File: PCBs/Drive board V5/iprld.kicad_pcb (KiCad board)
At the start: 2 copper layers, 17 parts, among them J1 Conn_01x02, J2 Conn_02x01, J3 Conn_02x02_Top_Bottom, U1 TJA1051T-3, U15 AMS1117-3.3

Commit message: Updated drive board
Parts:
- removed C14, C26: 10u, Capacitor_SMD:C_0805_2012Metric
- removed C15: 1u, Capacitor_SMD:C_0805_2012Metric
- removed C21: 0.1u, Capacitor_SMD:C_0805_2012Metric
- removed U15: AMS1117-3.3, Package_TO_SOT_SMD:SOT-223-3_TabPin2
- added C3: 0.1u, Capacitor_SMD:C_0805_2012Metric, F.Cu at (43.0, 54.8)
- moved G*** 45.6 mm to (102.0, 97.2)
- moved C1 20.0 mm to (43.0, 50.2), turned to 0 degrees
- moved J3 15.4 mm to (103.0, 28.1)
- moved J1 13.3 mm to (91.5, 32.2)
- moved U1 12.9 mm to (41.3, 42.0), turned to 90 degrees
- moved C2 11.9 mm to (45.5, 34.2)
- moved J2 3.50 mm to (39.0, 28.1)
- moved U2 0.67 mm to (76.4, 66.4)
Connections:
- net /CANH renamed /CAN_P
- net /CANL renamed /CAN_N
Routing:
- net +3.3V: track 114.2 -> 50.0 mm, vias 1 -> 0
- net GND: track 49.2 -> 5.37 mm, vias 11 -> 3
- net /CAN_S: track 38.1 -> 0.00 mm
- net +5V: track 90.4 -> 71.0 mm, vias 0 -> 1
- net /CAN_RX: track 38.7 -> 21.1 mm
- net /M3: track 22.4 -> 33.9 mm
- net /M2: track 29.2 -> 40.1 mm
- net /M4: track 31.3 -> 40.1 mm
- net /CAN_N: track 6.53 -> 13.4 mm
- net /M1: track 30.5 -> 37.3 mm
- net /CAN_TX: track 25.9 -> 19.8 mm, vias 0 -> 1
- net /CAN_P: track 6.63 -> 9.14 mm

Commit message: Drive v5 changes
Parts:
- moved G*** 41.0 mm to (100.8, 56.2)
- moved H2 40.1 mm to (25.0, 73.5)
- moved H3 39.8 mm to (115.0, 73.8)
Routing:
- net /CAN_S: track 0.00 -> 37.7 mm, vias 0 -> 1
- net GND: track 5.37 -> 7.39 mm, vias 3 -> 4
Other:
- board outline added: 100 x 60 mm
- board text added: "CAN H"
- board text added: "CAN L"
- board text added: "Drive Board by Max Ryan :)"
- board text added: "Pineapple on pizza should be a crime"
- board text removed: "Drive Board by Max Ryan"
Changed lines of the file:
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@@
 	(footprint "footprints:IPRL_31mm"
 		(layer "F.Cu")
-		(at 102 97.25)
+		(at 100.75 56.25)
 		(property "Reference" "G***"
 			(at 0 0 0)
@@
 			(at -0.5 6.4 0)
 			(layer "F.SilkS")
+			(hide yes)
 			(effects
 				(font
@@
 			(at -2.75 -9.75 0)
 			(layer "F.SilkS")
+			(hide yes)
 			(effects
 				(font
@@
 	(footprint "MountingHole:MountingHole_3.2mm_M3_Pad_TopBottom"
 		(layer "F.Cu")
-		(at 25 113.6)
+		(at 25 73.5)
 		(descr "Mounting Hole 3.2mm, M3, generated by kicad-footprint-generator mountinghole.py")
 		(tags "mountinghole M3")
@@
 			(at 0 -4.15 0)
 			(layer "F.SilkS")
+			(hide yes)
 			(effects
 				(font
@@
 			(at 0 6.4 0)
 			(layer "F.SilkS")
+			(hide yes)
 			(effects
 				(font
@@
 	(footprint "MountingHole:MountingHole_3.2mm_M3_Pad_TopBottom"
 		(layer "F.Cu")
-		(at 115 113.6)
+		(at 115 73.75)
 		(descr "Mounting Hole 3.2mm, M3, generated by kicad-footprint-generator mountinghole.py")
 		(tags "mountinghole M3")
@@
 			(at 0 -4.15 0)
 			(layer "F.SilkS")
+			(hide yes)
 			(effects
 				(font
@@
 		(embedded_fonts no)
 	)
-	(gr_line
-		(start 20 18.6)
-		(end 25 18.6)
-		(stroke
-			(width 0.2)
-			(type default)
-		)
-		(layer "F.Cu")
-	)
-	(gr_line
-		(start 20 118.6)
-		(end 25 118.6)
-		(stroke
-			(width 0.2)
-			(type default)
-		)
-		(layer "F.Cu")
-	)
-	(gr_line
-		(start 120 18.6)
-		(end 114.9 18.6)
-		(stroke
-			(width 0.2)
-			(type default)
-		)
-		(layer "F.Cu")
-	)
-	(gr_line
-		(start 25 118.6)
-		(end 25 113.6)
-		(stroke
-			(width 0.2)
-			(type default)
-		)
-		(layer "F.Cu")
-	)
-	(gr_line
-		(start 120 118.6)
-		(end 115 118.6)
-		(stroke
-			(width 0.2)
-			(type default)
-		)
-		(layer "F.Cu")
-	)
-	(gr_line
-		(start 25 18.6)
-		(end 25 23.6)
-		(stroke
-			(width 0.2)
-			(type default)
-		)
-		(layer "F.Cu")
-	)
 	(gr_rect
 		(start 20 18.6)
-		(end 120 118.6)
+		(end 120 78.6)
 		(stroke
 			(width 0.2)
-			(type default)
+			(type solid)
 		)
 		(fill no)
-		(layer "F.Cu")
+		(layer "Edge.Cuts")
 	)
-	(gr_line
-		(start 115 118.6)
-		(end 115 113.6)
-		(stroke
-			(width 0.2)
-			(type default)
+	(gr_text "Pineapple \non pizza \nshould be \na crime"
+		(at 85.25 26.25 0)
+		(layer "F.SilkS")
+		(effects
+			(font
+				(size 1 1)
+				(thickness 0.1)
+			)
+			(justify left bottom)
 		)
-		(layer "F.Cu")
 	)
-	(gr_line
-		(start 120 23.6)
-		(end 115 23.6)
-		(stroke
-			(width 0.2)
-			(type default)
+	(gr_text "Drive Board\nby Max Ryan :)"
+		(at 91 72 0)
+		(layer "F.SilkS")
+		(effects
+			(font
+				(size 1.5 1.5)
+				(thickness 0.3)
+				(bold yes)
+			)
+			(justify left bottom)
 		)
-		(layer "F.Cu")
 	)
-	(gr_line
-		(start 120 18.6)
-		(end 120 23.6)
-		(stroke
-			(width 0.2)
-			(type default)
+	(gr_text "CAN L\n"
+		(at 42.685 28.25 0)
+		(layer "F.SilkS")
+		(effects
+			(font
+				(size 1 1)
+				(thickness 0.1)
+			)
+			(justify left bottom)
 		)
-		(layer "F.Cu")
 	)
-	(gr_text "Drive Board\nby Max Ryan"
-		(at 93.5 116 0)
+	(gr_text "CAN H\n"
+		(at 32.75 31.75 0)
 		(layer "F.SilkS")
 		(effects
 			(font
-				(size 1.5 1.5)
-				(thickness 0.3)
-				(bold yes)
+				(size 1 1)
+				(thickness 0.1)
 			)
 			(justify left bottom)
@@
 	)
 	(segment
+		(start 46.45 34.25)
+		(end 46.45 32.3)
+		(width 0.2)
+		(layer "F.Cu")
+		(net 1)
+	)
+	(segment
 		(start 43.95 50.25)
 		(end 45.25 50.25)
@@
 	)
 	(segment
+		(start 46.45 32.3)
+		(end 46.5 32.25)
+		(width 0.2)
+		(layer "F.Cu")
+		(net 1)
+	)
+	(segment
 		(start 44 54.75)
 		(end 45.5 54.75)
@@
 	)
 	(via
+		(at 46.5 32.25)
+		(size 0.6)
+		(drill 0.3)
+		(layers "F.Cu" "B.Cu")
+		(net 1)
+	)
+	(via
 		(at 40.75 47)
 		(size 0.6)
@@
 	(segment
 		(start 39.45 32.106339)
-		(end 39.45 36.97)
+		(end 40.051 31.505339)
 		(width 0.2)
 		(layer "F.Cu")
@@
 	)
 	(segment
-		(start 41.311 38.831)
-		(end 41.98 39.5)
+		(start 39.45 28.52)
+		(end 39 28.07)
 		(width 0.2)
 		(layer "F.Cu")
@@
 	)
 	(segment
-		(start 39.45 36.97)
-		(end 40.704 38.224)
+		(start 40.704 38.224)
+		(end 39.45 36.97)
 		(width 0.2)
 		(layer "F.Cu")
@@
 	)
 	(segment
-		(start 41.050968 38.224)
-		(end 41.311 38.484032)
+		(start 40.051 31.505339)
+		(end 40.051 30.634661)
 		(width 0.2)
 		(layer "F.Cu")
@@
 	)
 	(segment
-		(start 40.051 31.505339)
-		(end 39.45 32.106339)
+		(start 41.311 38.831)
+		(end 41.311 38.484032)
 		(width 0.2)
 		(layer "F.Cu")
@@
 	)
 	(segment
-		(start 39 28.07)
-		(end 39.45 28.52)
+		(start 41.98 39.5)
+		(end 41.311 38.831)
 		(width 0.2)
 		(layer "F.Cu")
@@
 	)
 	(segment
-		(start 39.45 28.52)
-		(end 39.45 30.033661)
+		(start 41.050968 38.224)
+		(end 40.704 38.224)
 		(width 0.2)
 		(layer "F.Cu")
@@
 	(segment
 		(start 39.45 30.033661)
-		(end 40.051 30.634661)
+		(end 39.45 28.52)
 		(width 0.2)
 		(layer "F.Cu")
@@
 	)
 	(segment
-		(start 40.704 38.224)
+		(start 39.45 35.27492)
+		(end 39.45 32.106339)
+		(width 0.2)
+		(layer "F.Cu")
+		(net 19)
+	)
+	(segment
+		(start 41.311 38.484032)
 		(end 41.050968 38.224)
 		(width 0.2)
@@
 	)
 	(segment
-		(start 40.051 30.634661)
-		(end 40.051 31.505339)
+		(start 39.45 36.97)
+		(end 39.45 35.27492)
 		(width 0.2)
 		(layer "F.Cu")
@@
 	)
 	(segment
-		(start 41.311 38.484032)
-		(end 41.311 38.831)
+		(start 40.051 30.634661)
+		(end 39.45 30.033661)
 		(width 0.2)
 		(layer "F.Cu")
@@
 	)
 	(segment
-		(start 39 31.07)
+		(start 40.43597 38.592367)
 		(end 39 37.156397)
 		(width 0.2)
@@
 	)
 	(segment
-		(start 39 37.156397)
+		(start 39 35.27492)
+		(end 39 31.07)
+		(width 0.2)
+		(layer "F.Cu")
+		(net 20)
+	)
+	(segment
+		(start 40.71 39.5)
 		(end 40.71 38.866397)
 		(width 0.2)
@@
 	)
 	(segment
+		(start 39 37.156397)
+		(end 39 35.27492)
+		(width 0.2)
+		(layer "F.Cu")
+		(net 20)
+	)
+	(segment
 		(start 40.71 38.866397)
-		(end 40.71 39.5)
+		(end 40.43597 38.592367)
 		(width 0.2)
 		(layer "F.Cu")
@@
 	)
 	(segment
+		(start 39.44 39.5)
+		(end 36 42.94)
+		(width 0.2)
+		(layer "F.Cu")
+		(net 26)
+	)
+	(segment
+		(start 36 42.94)
+		(end 36 43.5)
+		(width 0.2)
+		(layer "F.Cu")
+		(net 26)
+	)
+	(via
+		(at 36 43.5)
+		(size 0.6)
+		(drill 0.3)
+		(layers "F.Cu" "B.Cu")
+		(net 26)
+	)
+	(segment
+		(start 36 43.5)
+		(end 36 54.25)
+		(width 0.2)
+		(layer "B.Cu")
+		(net 26)
+	)
+	(segment
+		(start 36 54.25)
+		(end 45.62 63.87)
+		(width 0.2)
+		(layer "B.Cu")
+		(net 26)
+	)
+	(segment
+		(start 45.62 63.87)
+		(end 53.5 63.87)
+		(width 0.2)
+		(layer "B.Cu")
+		(net 26)
+	)
+	(segment
 		(start 50 57.83)
 		(end 53.5 61.33)
@@
 		)
 	)
+	(generated
+		(type tuning_pattern)
+		(name "Tuning Pattern")
+		(layer "F.Cu")
+		(base_line
+			(pts
+				(xy 40.43597 38.592367) (xy 39 37.156397) (xy 39 35.27492)
+			)
+		)
+		(base_line_coupled
+			(pts
+				(xy 40.704 38.224) (xy 39.45 36.97) (xy 39.45 35.27492)
+			)
+		)
+		(corner_radius_percent 80)
+		(end
+			(xy 39 35.27492)
+		)
+		(initial_side "left")
+		(last_diff_pair_gap 0.25)
+		(last_netname "/CAN_P")
+		(last_status "tuned")
+		(last_track_width 0.2)
+		(last_tuning "13.3037 mm (tuned)")
+		(max_amplitude 1)
+		(min_amplitude 0.2)
+		(min_spacing 1)
+		(origin
+			(xy 40.43597 38.592367)
+		)
+		(override_custom_rules no)
+		(rounded yes)
+		(single_sided no)
+		(target_length 1000000)
+		(target_length_max 1000000)
+		(target_length_min 0)
+		(target_skew 0)
+		(target_skew_max 0.1)
+		(target_skew_min -0.1)
+		(tuning_mode "diff_pair")
+		(members "356f25eb-2dce-41ec-9833-14f512c0acfb" "38f040bc-6008-4836-886b-c5aaa7f139b5"
+			"bcd30e06-786a-4961-932b-d6303e9b7a0b" "eff296ab-6fed-4a58-92bb-c176535c685c"
+		)
+	)

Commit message: Updates drive board
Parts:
- added G***: LOGO, LOGO, F.Cu at (37.3, 73.0)
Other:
- board text added: "What went wrong?"
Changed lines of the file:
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@@
+		(embedded_fonts no)
+	)
+	(footprint "LOGO"
+		(layer "F.Cu")
+		(at 37.306739 72.985484)
+		(property "Reference" "G***"
+			(at -1.5 -4.75 0)
+			(layer "F.SilkS")
+			(hide yes)
+			(effects
+				(font
+					(size 1.5 1.5)
+					(thickness 0.3)
+				)
+			)
+		)
+		(property "Value" "LOGO"
+			(at 0.75 0 0)
+			(layer "F.SilkS")
+			(hide yes)
+			(effects
+				(font
+					(size 1.5 1.5)
+					(thickness 0.3)
+				)
+			)
+		)
+		(property "Datasheet" ""
+			(at 0 0 0)
+			(layer "F.Fab")
+			(hide yes)
+			(effects
+				(font
+					(size 1.27 1.27)
+					(thickness 0.15)
+				)
+			)
+		)
+		(property "Description" ""
+			(at 0 0 0)
+			(layer "F.Fab")
+			(hide yes)
+			(effects
+				(font
+					(size 1.27 1.27)
+					(thickness 0.15)
+				)
+			)
+		)
+		(attr board_only exclude_from_pos_files exclude_from_bom)
+		(fp_poly
+			(pts
+				(xy -4.444145 4.932513) (xy -4.444145 5.000884) (xy -4.722515 5.000884) (xy -5.000884 5.000884)
+				(xy -5.000884 4.932513) (xy -5.000884 4.864141) (xy -4.722515 4.864141) (xy -4.444145 4.864141)
+			)
+			(stroke
+				(width 0)
+				(type solid)
+			)
+			(fill yes)
+			(layer "F.SilkS")
+		)
+		(fp_poly
+			(pts
+				(xy -3.61392 4.512517) (xy -3.61392 4.580888) (xy -3.889848 4.580888) (xy -4.165776 4.580888) (xy -4.165776 4.512517)
+				(xy -4.165776 4.444145) (xy -3.889848 4.444145) (xy -3.61392 4.444145)
+			)
+			(stroke
+				(width 0)
+				(type solid)
+			)
+			(fill yes)
+			(layer "F.SilkS")
+		)
+		(fp_poly
+			(pts
+				(xy -2.778812 3.960661) (xy -2.778812 4.029033) (xy -3.889848 4.029033) (xy -5.000884 4.029033)
+				(xy -5.000884 3.960661) (xy -5.000884 3.89229) (xy -3.889848 3.89229) (xy -2.778812 3.89229)
+			)
+			(stroke
+				(width 0)
+				(type solid)
+			)
+			(fill yes)
+			(layer "F.SilkS")
+		)
+		(fp_poly
+			(pts
+				(xy -2.778812 4.932513) (xy -2.778812 5.000884) (xy -2.917997 5.000884) (xy -3.057181 5.000884)
+				(xy -3.057181 4.932513) (xy -3.057181 4.864141) (xy -2.917997 4.864141) (xy -2.778812 4.864141)
+			)
+			(stroke
+				(width 0)
+				(type solid)
+			)
+			(fill yes)
+			(layer "F.SilkS")
+		)
+		(fp_poly
+			(pts
+				(xy 0.830225 4.790886) (xy 0.830225 4.859258) (xy 0.761853 4.859258) (xy 0.693482 4.859258) (xy 0.693482 4.790886)
+				(xy 0.693482 4.722515) (xy 0.761853 4.722515) (xy 0.830225 4.722515)
+			)
+			(stroke
+				(width 0)
+				(type solid)
+			)
+			(fill yes)
+			(layer "F.SilkS")
+		)
+		(fp_poly
+			(pts
+				(xy 2.222073 4.932513) (xy 2.222073 5.000884) (xy 1.946145 5.000884) (xy 1.670217 5.000884) (xy 1.670217 4.932513)
+				(xy 1.670217 4.864141) (xy 1.946145 4.864141) (xy 2.222073 4.864141)
+			)
+			(stroke
+				(width 0)
+				(type solid)
+			)
+			(fill yes)
+			(layer "F.SilkS")
+		)
+		(fp_poly
+			(pts
+				(xy 3.057181 4.375774) (xy 3.057181 4.444145) (xy 2.849625 4.444145) (xy 2.642069 4.444145) (xy 2.642069 4.375774)
+				(xy 2.642069 4.307402) (xy 2.849625 4.307402) (xy 3.057181 4.307402)
+			)
+			(stroke
+				(width 0)
+				(type solid)
+			)
+			(fill yes)
+			(layer "F.SilkS")
+		)
+		(fp_poly
+			(pts
+				(xy 3.887406 3.960661) (xy 3.887406 4.029033) (xy 1.943703 4.029033) (xy 0 4.029033) (xy 0 3.960661)
+				(xy 0 3.89229) (xy 1.943703 3.89229) (xy 3.887406 3.89229)
+			)
+			(stroke
+				(width 0)
+				(type solid)
+			)
+			(fill yes)
+			(layer "F.SilkS")
+		)
+		(fp_poly
+			(pts
+				(xy 1.665334 -0.832667) (xy 1.665334 -0.693482) (xy 1.804518 -0.693482) (xy 1.943703 -0.693482)
+				(xy 1.943703 -0.068372) (xy 1.943703 0.556739) (xy 1.250221 0.556739) (xy 0.556739 0.556739) (xy 0.556739 0.695924)
+				(xy 0.556739 0.835109) (xy 0.971852 0.835109) (xy 1.386964 0.835109) (xy 1.386964 0.971852) (xy 1.386964 1.108594)
+				(xy 0.832667 1.108594) (xy 0.278369 1.108594) (xy 0.278369 1.389406) (xy 0.278369 1.670217) (xy 0.554297 1.670217)
+				(xy 0.830225 1.670217) (xy 0.830225 1.946145) (xy 0.830225 2.222073) (xy 0.693482 2.222073) (xy 0.556739 2.222073)
+				(xy 0.556739 2.082888) (xy 0.556739 1.943703) (xy 0.417554 1.943703) (xy 0.278369 1.943703) (xy 0.278369 2.429629)
+				(xy 0.278369 2.915555) (xy 0.139185 2.915555) (xy 0 2.915555) (xy 0 3.123035) (xy 0 3.330515) (xy -0.137964 3.331812)
+				(xy -0.275928 3.333109) (xy -0.277225 3.471073) (xy -0.278522 3.609037) (xy -0.41763 3.609037) (xy -0.556739 3.609037)
+				(xy -0.556739 4.165776) (xy -0.556739 4.722515) (xy -0.417554 4.722515) (xy -0.27837 4.722515) (xy -0.27837 4.8617)
+				(xy -0.27837 5.000884) (xy -0.55427 5.000884) (xy -0.83017 5.000884) (xy -0.831419 4.584551) (xy -0.832667 4.168218)
+				(xy -0.970555 4.166921) (xy -1.108443 4.165624) (xy -1.10974 4.027736) (xy -1.111036 3.889848) (xy -1.250221 3.889848)
+				(xy -1.389406 3.889848) (xy -1.390703 4.027736) (xy -1.392 4.165624) (xy -1.529888 4.166921) (xy -1.667775 4.168218)
+				(xy -1.669072 4.306181) (xy -1.670369 4.444145) (xy -1.807036 4.444145) (xy -1.943703 4.444145)
+				(xy -1.943703 4.58333) (xy -1.943703 4.722515) (xy -1.80696 4.722515) (xy -1.670217 4.722515) (xy -1.670217 4.8617)
+				(xy -1.670217 5.000884) (xy -1.946145 5.000884) (xy -2.222073 5.000884) (xy -2.222073 4.444145)
+				(xy -2.222073 3.887406) (xy -2.361258 3.887406) (xy -2.500442 3.887406) (xy -2.500442 3.748221)
+				(xy -2.500442 3.609037) (xy -2.639627 3.609037) (xy -2.778812 3.609037) (xy -2.778812 3.469852)
+				(xy -2.778812 3.330667) (xy -2.917997 3.330667) (xy -3.057181 3.330667) (xy -3.057181 3.193924)
+				(xy -3.057181 3.057181) (xy -3.193924 3.057181) (xy -3.330667 3.057181) (xy -3.330667 2.917996)
+				(xy -3.330667 2.778812) (xy -3.469852 2.778812) (xy -3.609037 2.778812) (xy -3.609037 1.946145)
+				(xy -3.609037 1.113478) (xy -3.472334 1.113478) (xy -3.335632 1.113478) (xy -3.33437 1.390627) (xy -3.333109 1.667775)
+				(xy -3.195145 1.669072) (xy -3.057181 1.670369) (xy -3.057181 1.807036) (xy -3.057181 1.943703)
+				(xy -2.917997 1.943703) (xy -2.778812 1.943703) (xy -2.778812 2.082888) (xy -2.778812 2.222073)
+				(xy -2.500442 2.222073) (xy -2.222073 2.222073) (xy -2.222073 2.082888) (xy -2.222073 1.943703)
+				(xy -2.082888 1.943703) (xy -1.943703 1.943703) (xy -1.943703 1.80696) (xy -1.943703 1.670217) (xy -1.736147 1.670217)
+				(xy -1.528591 1.670217) (xy -1.528591 1.531085) (xy -1.528591 1.391953) (xy -1.319814 1.390679)
+				(xy -1.111036 1.389406) (xy -1.10974 1.251518) (xy -1.108443 1.11363) (xy -0.970555 1.112333) (xy -0.832667 1.111036)
+				(xy -0.831433 0.208777) (xy -0.830576 -0.417554) (xy -0.27837 -0.417554) (xy -0.27837 -0.27837)
+				(xy -0.139185 -0.27837) (xy 0 -0.27837) (xy 0 -0.417554) (xy 0 -0.556739) (xy -0.139185 -0.556739)
+				(xy -0.27837 -0.556739) (xy -0.27837 -0.417554) (xy -0.830576 -0.417554) (xy -0.830199 -0.693482)
+				(xy -0.693469 -0.693482) (xy -0.556739 -0.693482) (xy -0.556739 -0.832667) (xy -0.556739 -0.971852)
+				(xy 0.554297 -0.971852) (xy 1.665334 -0.971852)
+			)
+			(stroke
+				(width 0)
+				(type solid)
+			)
+			(fill yes)
+			(layer "F.SilkS")
+		)
 		(embedded_fonts no)
 	)
@@
 			)
 			(justify left bottom)
+		)
+	)
+	(gr_text "What went \nwrong?"
+		(at 39.5 42.25 0)
+		(layer "F.SilkS")
+		(effects
+			(font
+				(size 0.5 0.5)
+				(thickness 0.1)
+			)
+			(justify left bottom)

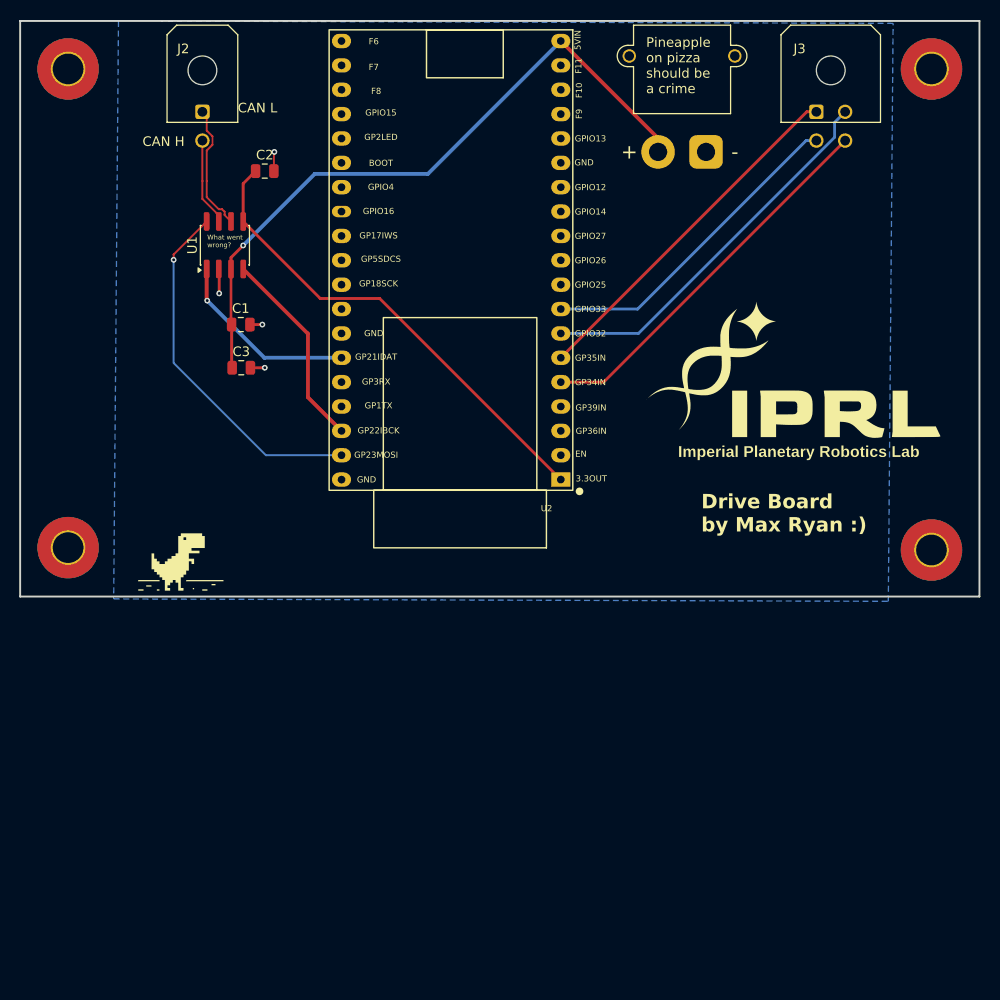
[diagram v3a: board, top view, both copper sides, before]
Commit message: Fixed drive board
had pwm on input only pins :(
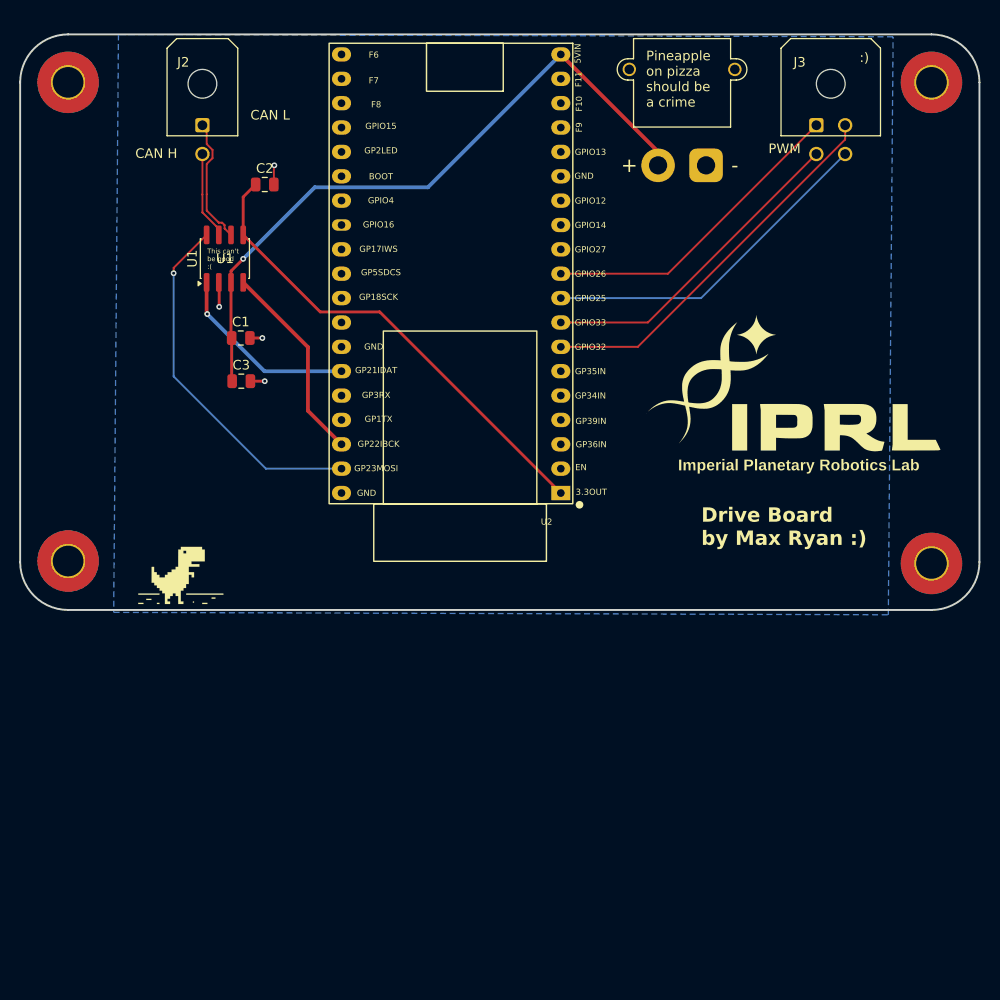
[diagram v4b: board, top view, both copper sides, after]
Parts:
- moved G*** 1.40 mm to (37.3, 74.4)
- moved H2 1.40 mm to (25.0, 74.9)
- moved H3 1.40 mm to (115.0, 75.2)
- moved U2 1.40 mm to (76.4, 67.8)
- moved C1 1.40 mm to (43.0, 51.6)
- moved C2 1.40 mm to (45.5, 35.6)
- moved C3 1.40 mm to (43.0, 56.1)
- moved G*** 1.40 mm to (100.8, 57.6)
- moved H1 1.40 mm to (25.0, 25.0)
- moved H4 1.40 mm to (115.0, 25.0)
- moved J1 1.40 mm to (91.5, 33.6)
- moved J2 1.40 mm to (39.0, 29.5)
- moved J3 1.40 mm to (103.0, 29.5)
- moved U1 1.40 mm to (41.3, 43.4)
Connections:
- U2 pad 10: unconnected-(U2-GPIO26-Pad10) -> /M1
- U2 pad 5: /M4 -> unconnected-(U2-GPIO34-Pad5)
- U2 pad 6: /M1 -> unconnected-(U2-GPIO35-Pad6)
- U2 pad 9: unconnected-(U2-GPIO25-Pad9) -> /M4
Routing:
- net /M4: track 40.1 -> 35.9 mm
- net /M1: track 37.3 -> 33.1 mm
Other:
- outline, holes or cut-outs redrawn
- board text added: ":)"
- board text added: "PWM"
- board text added: "This can't be good :("
- board text removed: "What went wrong?"
